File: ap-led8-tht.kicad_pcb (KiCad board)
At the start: 2 copper layers, 36.3 x 16.1 mm, 12 parts, among them J1 Conn_01x08_Socket, J2 Conn_01x08_Socket

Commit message: PCB: add front GND zone
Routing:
- added copper zone on F.Cu, net GND
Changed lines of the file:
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@@
   (segment (start 86.36 62.23) (end 86.36 56.515) (width 0.3048) (layer "B.Cu") (net 9))
   (segment (start 85.09 63.5) (end 86.36 62.23) (width 0.3048) (layer "B.Cu") (net 9))
+  (zone (net 1) (net_name "GND") (layer "F.Cu") (hatch edge 0.5)
+    (connect_pads (clearance 0.5))
+    (min_thickness 0.25) (filled_areas_thickness no)
+    (fill yes (thermal_gap 0.5) (thermal_bridge_width 0.5))
+    (polygon
+      (pts
+        (xy 77.851 48.133)
+        (xy 115.316 48.133)
+        (xy 115.316 65.913)
+        (xy 77.851 65.913)
+      )
+    )
+  )
 )

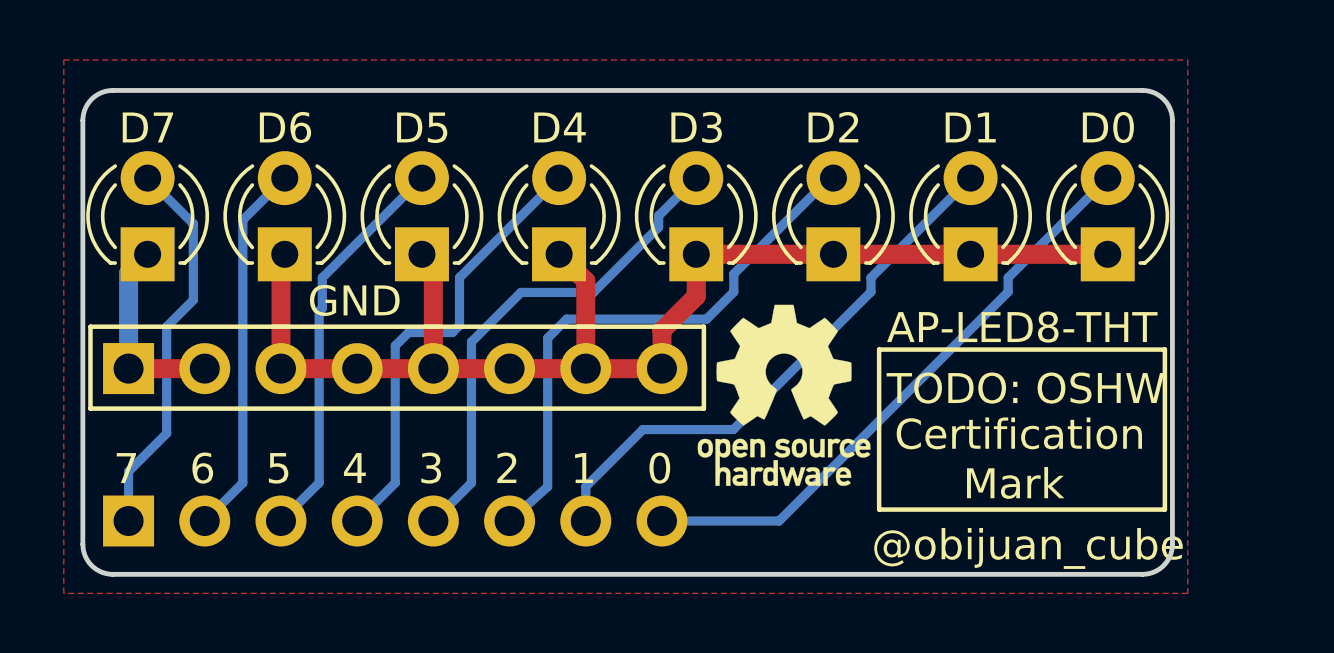
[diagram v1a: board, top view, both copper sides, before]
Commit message: PCB: fixed DRC warnings
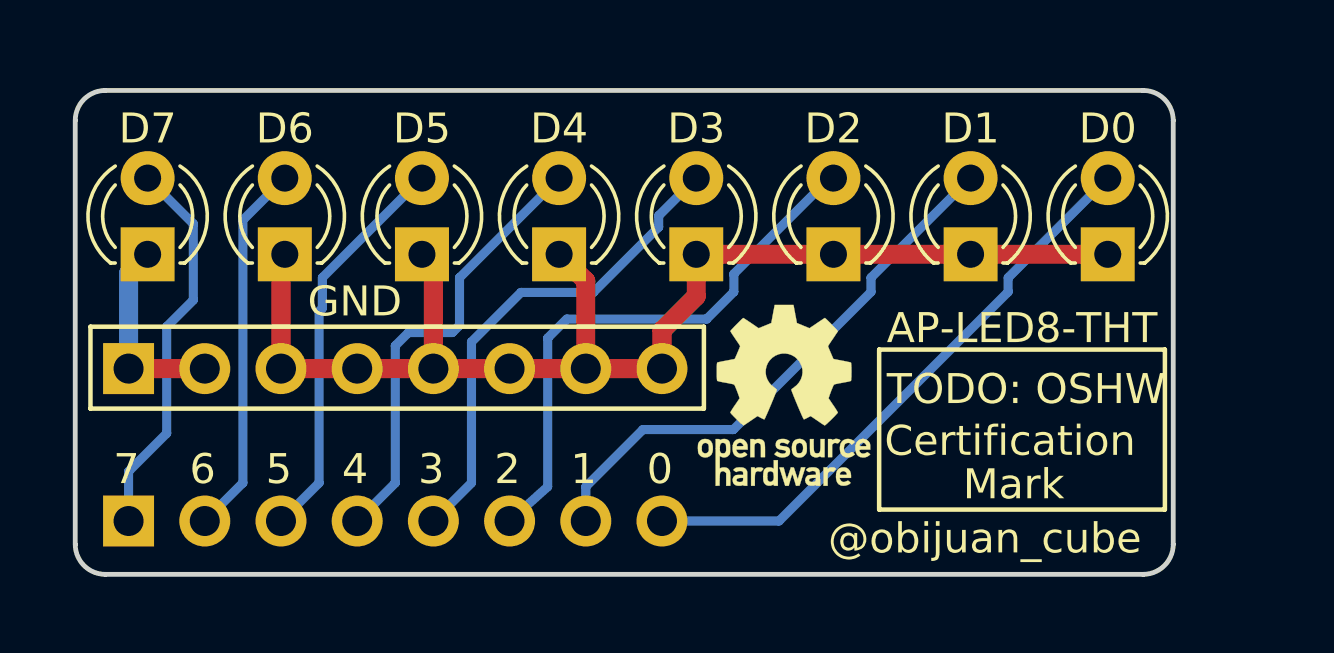
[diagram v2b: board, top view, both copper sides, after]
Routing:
- removed copper zone on F.Cu, net GND
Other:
- board size 36.3 x 16.1 mm -> 36.6 x 16.1 mm

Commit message: PCB: New GND zone
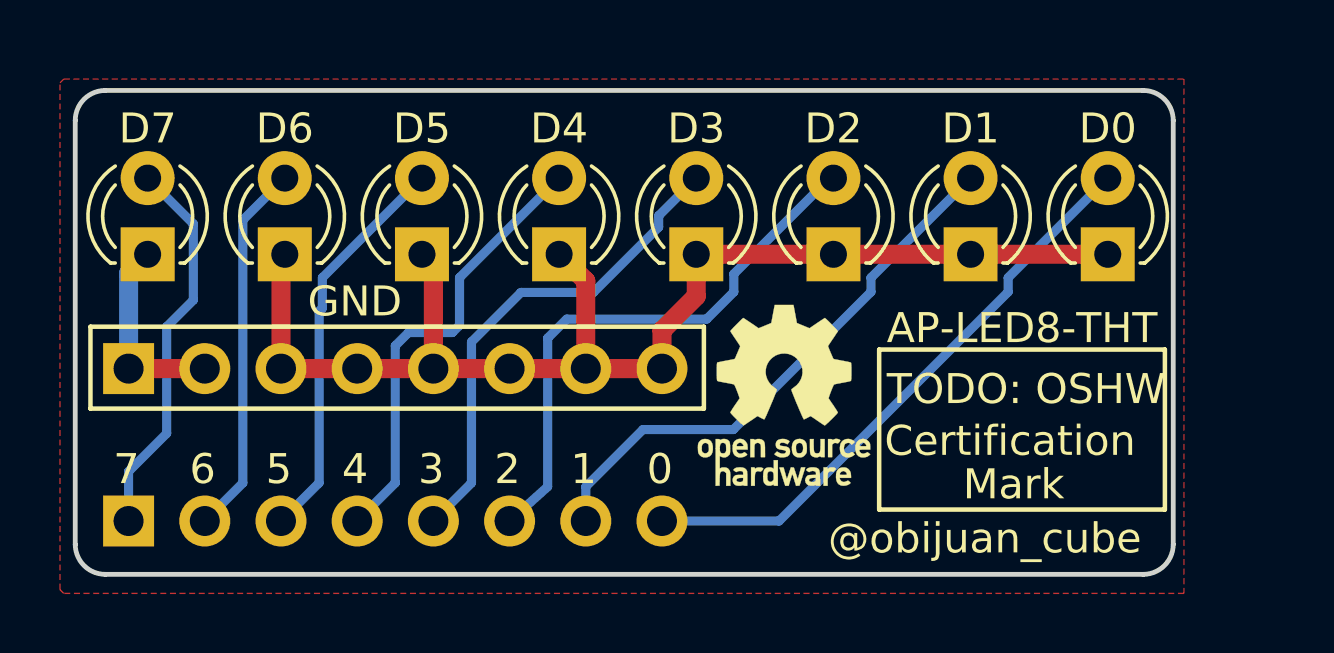
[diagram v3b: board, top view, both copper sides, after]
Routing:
- added copper zone on F.Cu, net GND
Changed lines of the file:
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@@
   (segment (start 86.36 62.23) (end 86.36 56.515) (width 0.3048) (layer "B.Cu") (net 9))
   (segment (start 85.09 63.5) (end 86.36 62.23) (width 0.3048) (layer "B.Cu") (net 9))
+  (zone (net 1) (net_name "GND") (layer "F.Cu") (hatch edge 0.5)
+    (connect_pads (clearance 0.5))
+    (min_thickness 0.25) (filled_areas_thickness no)
+    (fill yes (thermal_gap 0.5) (thermal_bridge_width 0.5))
+    (polygon
+      (pts
+        (xy 77.851 48.768)
+        (xy 115.189 48.768)
+        (xy 115.189 65.913)
+        (xy 77.851 65.913)
+        (xy 77.724 65.786)
+        (xy 77.724 48.895)
+      )
+    )
+  )
 )
